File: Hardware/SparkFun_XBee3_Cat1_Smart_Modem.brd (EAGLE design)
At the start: 45.7 x 63.5 mm, 132 parts, among them J4 QWIIC_RIGHT_ANGLE, Q2 3.1A/30V/105mΩ, U1 FSUSB30MUX_MSOP10, U2 AP63203, U3 ESD Diode, U5 ESD Diode, U6 CP210X

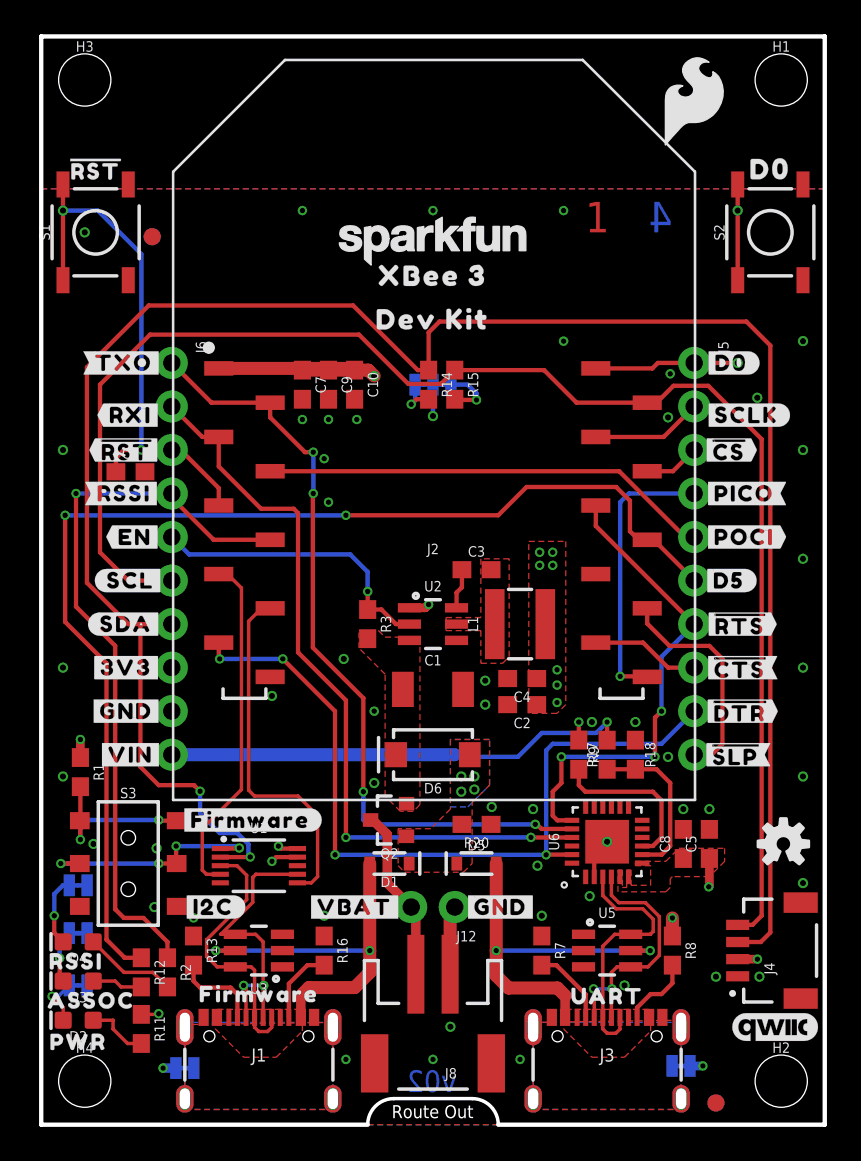
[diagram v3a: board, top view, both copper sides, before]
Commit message: NEW PINOUT - rearranges pinout to match module pinout directly
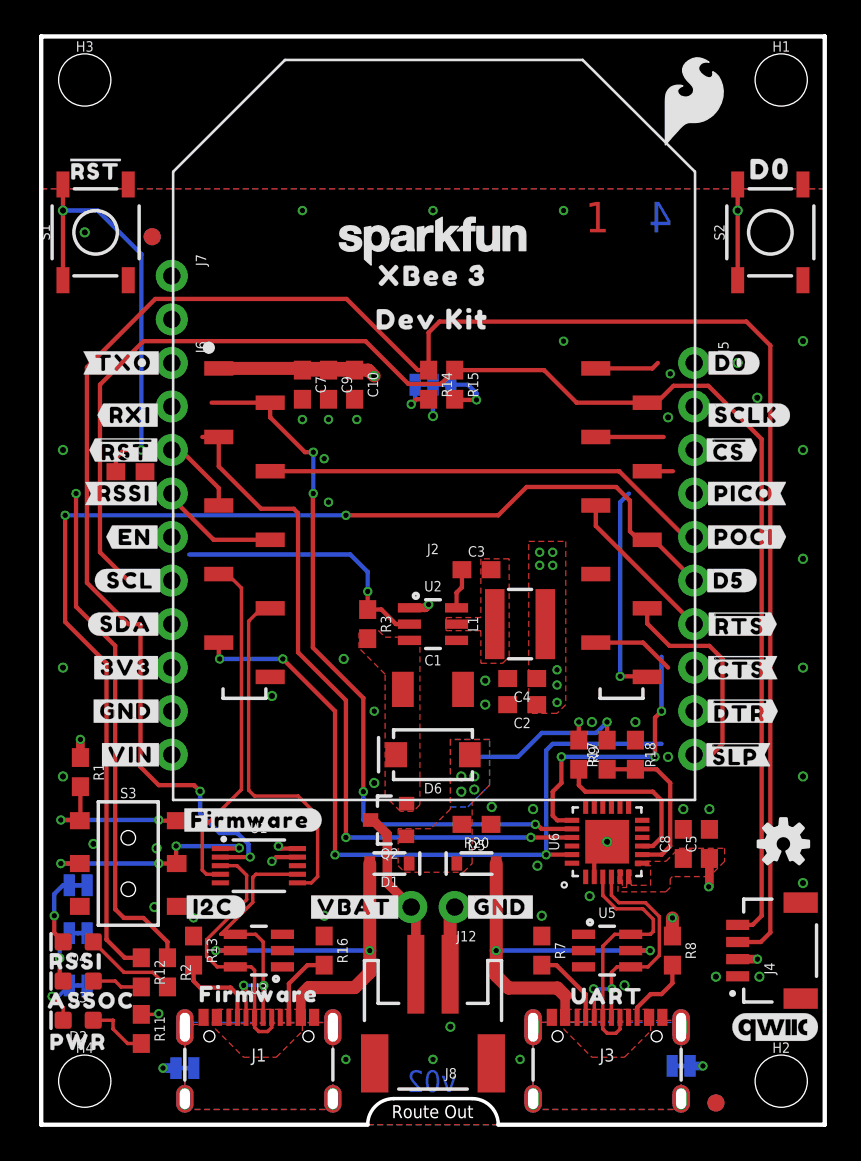
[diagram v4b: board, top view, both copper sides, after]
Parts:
- added J7: (no value), SparkFun-Connectors:1X02_NO_SILK
- moved U$64 4.76 mm to (2.16, 17.3), turned to 270 degrees
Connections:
- net !RESET!: now also J6.5; no longer J6.3
- net 3.3V: now also J6.1; no longer J6.8
- net D1/SCL: now also J5.2; no longer J6.6
- net D10/RSSI_PWM: now also J6.6; no longer J6.4
- net D12/SPI_POCI: now also J6.4; no longer J5.5
- net D13/TXO: now also J6.2; no longer J6.1
- net D14/RXI: now also J6.3; no longer J6.2
- net D2/SPI_CLK: now also J5.3; no longer J5.2
- net D3/SPI_!CS!: now also J5.4; no longer J5.3
- net D4/SPI_PICO: now also J5.10; no longer J5.4
- net D6/!RTS!: now also J5.5; no longer J5.7
- net D7/!CTS!: now also J5.9; no longer J5.8
- net D8/!DTR!: now also J6.9; no longer J5.9
- net D9/!SLEEP!: now also J5.8; no longer J5.10
- net EN: now also J7.1; no longer J6.5
- net GND: now also J6.10; no longer J6.9
- net VIN: now also J7.2; no longer J6.10
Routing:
- net VIN: track 25.8 -> 9.26 mm
- net D10/RSSI_PWM: track 42.6 -> 36.7 mm
- net D0: track 22.9 -> 18.2 mm
- net D4/SPI_PICO: track 16.3 -> 12.5 mm
- net D13/TXO: track 46.0 -> 42.7 mm
- net D1/SCL: track 87.9 -> 85.1 mm
- net D6/!RTS!: track 28.3 -> 25.6 mm
- net D8/!DTR!: track 46.9 -> 44.2 mm
- net D14/RXI: track 44.2 -> 41.7 mm
- net D2/SPI_CLK: track 6.48 -> 3.96 mm
- net !RESET!: track 31.6 -> 29.3 mm
- net D3/SPI_!CS!: track 3.25 -> 1.50 mm
- net D11/SDA: track 120.7 -> 119.1 mm
- net D7/!CTS!: track 6.34 -> 4.82 mm
- net EN: track 17.3 -> 15.8 mm
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
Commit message: Updates silk
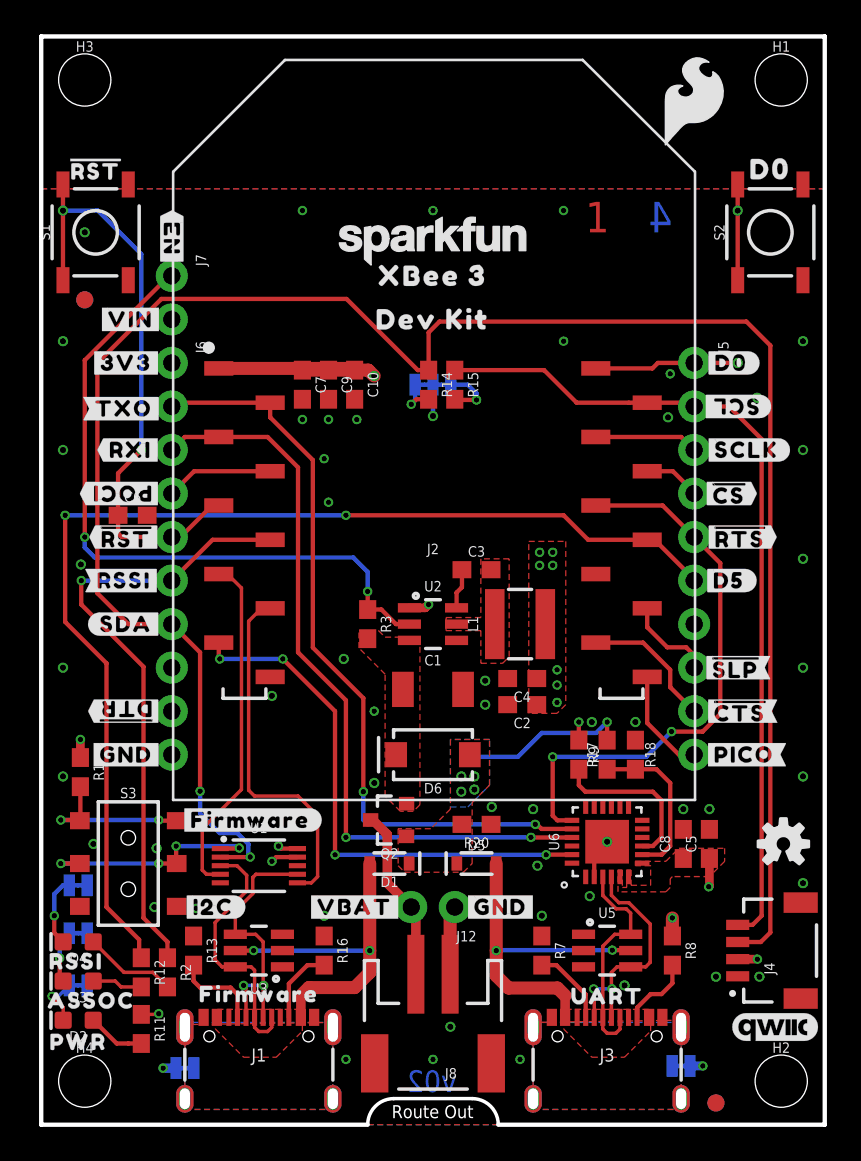
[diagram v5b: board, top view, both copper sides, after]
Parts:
- U$14: device top:#D12#POCI#23 -> top:#POCI#D12#24
- U$19: device top:#AD1#D1#7 -> top:#D1#AD1#8
- moved U$32 36.7 mm to (40.5, 41.9), turned to 180 degrees
- moved U$29 36.4 mm to (4.70, 36.8), turned to 180 degrees
- moved U$5 35.8 mm to (4.95, 24.1), turned to 180 degrees
- moved U$41 25.4 mm to (5.21, 47.0)
- moved U$46 25.4 mm to (10.0, 47.0)
- moved U$19 25.0 mm to (34.3, 41.9)
- moved U$59 22.4 mm to (11.6, 24.1)
- moved U$14 21.2 mm to (12.3, 36.8)
- moved U$44 17.8 mm to (10.3, 44.5)
- moved U$9 17.8 mm to (4.95, 44.5)
- moved U$24 17.5 mm to (7.62, 51.7), turned to 270 degrees
- moved U$21 15.2 mm to (9.78, 49.5)
- moved U$13 15.2 mm to (33.8, 21.6)
- moved U$28 15.2 mm to (41.0, 21.6)
- moved FD1 5.39 mm to (2.54, 48.1)
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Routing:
- net VIN: track 9.26 -> 52.2 mm
- net D1/SCL: track 85.1 -> 49.0 mm
- net EN: track 15.8 -> 40.1 mm, vias 1 -> 2
- net D12/SPI_POCI: track 25.8 -> 6.28 mm
- net D8/!DTR!: track 44.2 -> 36.4 mm
- net D6/!RTS!: track 25.6 -> 32.9 mm, vias 3 -> 2
- net D9/!SLEEP!: track 12.0 -> 5.24 mm
- net D4/SPI_PICO: track 12.5 -> 6.20 mm, vias 1 -> 0
- net !RESET!: track 29.3 -> 34.8 mm
- net D0: track 18.2 -> 22.9 mm
- net D7/!CTS!: track 4.82 -> 7.99 mm
- net D14/RXI: track 41.7 -> 44.4 mm
- net D+: track 15.3 -> 13.0 mm
- net V_USB_2: track 22.3 -> 20.0 mm
- net V_USB: track 22.4 -> 20.2 mm
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
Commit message: Updates a few labels
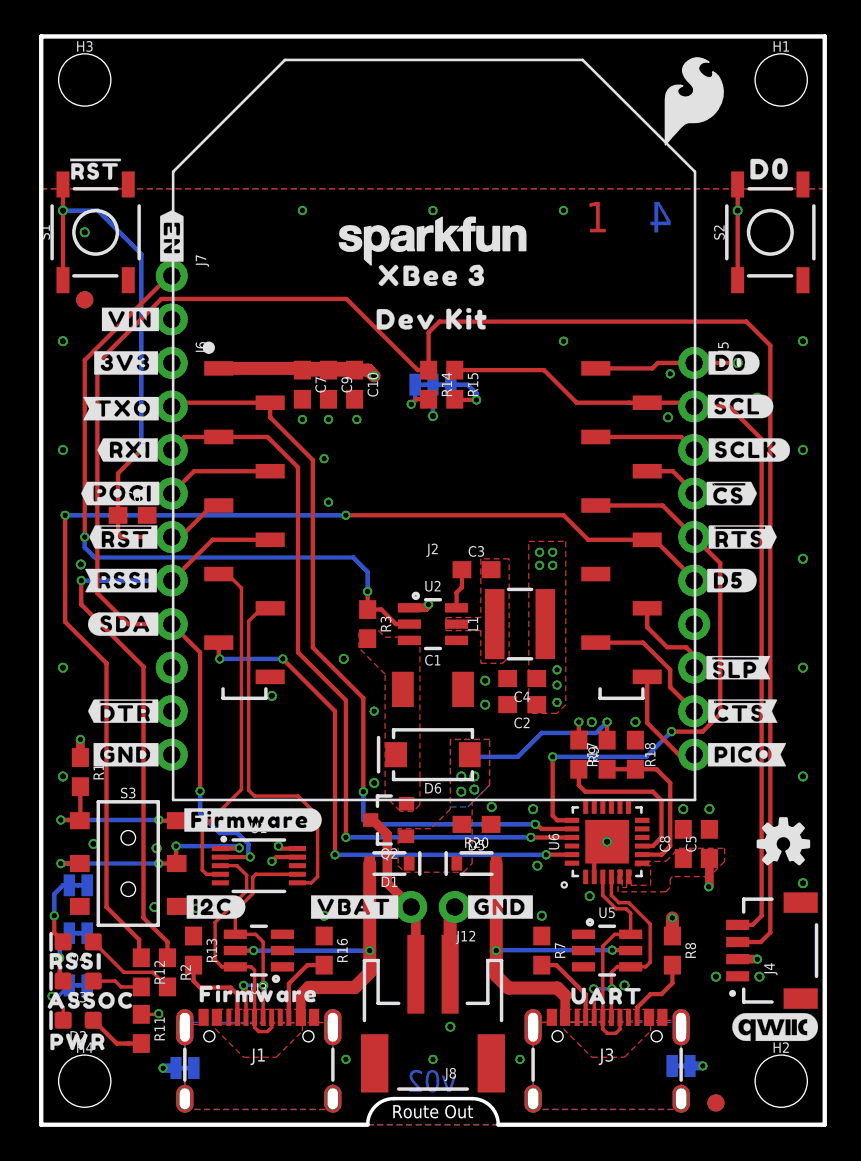
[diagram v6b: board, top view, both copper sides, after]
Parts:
- U$29: device top:#POCI#22 -> top:#POCI#23
- U$32: device top:#SCL#6 -> top:#SCL#7
- U$5: device top:##DTR##26 -> top:##DTR##27
- moved U$32 0.13 mm to (40.6, 41.9), turned to 0 degrees
- moved U$29 0.08 mm to (4.78, 36.8), turned to 0 degrees
- turned U$5 to 0 degrees
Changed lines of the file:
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@@
 <element name="U$3" library="top" package="##CS##19" value="" x="40.132" y="36.83" smashed="yes"/>
 <element name="U$4" library="top" package="##CTS##25" value="" x="40.767" y="24.13" smashed="yes"/>
-<element name="U$5" library="top" package="##DTR##26" value="" x="4.953" y="24.13" smashed="yes" rot="R180"/>
 <element name="U$7" library="top" package="##RTS##24" value="" x="40.767" y="34.29" smashed="yes"/>
 <element name="U$9" library="top" package="#3V3#1" value="" x="4.953" y="44.45" smashed="yes"/>
@@
 <element name="U$26" library="top" package="#I2C#33" value="" x="22.86" y="44.831" smashed="yes" rot="MR0"/>
 <element name="U$28" library="top" package="#PICO#23" value="" x="41.021" y="21.59" smashed="yes"/>
-<element name="U$29" library="top" package="#POCI#22" value="" x="4.699" y="36.83" smashed="yes" rot="R180"/>
 <element name="U$31" library="top" package="#RSSI#16" value="" x="4.826" y="31.75" smashed="yes"/>
-<element name="U$32" library="top" package="#SCL#6" value="" x="40.513" y="41.91" smashed="yes" rot="R180"/>
 <element name="U$33" library="top" package="#SCLK#18" value="" x="41.148" y="39.37" smashed="yes"/>
 <element name="U$34" library="top" package="#SDA#7" value="" x="4.953" y="29.21" smashed="yes"/>
@@
 <element name="U$19" library="top" package="#D1#AD1#8" value="" x="34.29" y="41.91" smashed="yes" rot="MR0"/>
 <element name="U$14" library="top" package="#POCI#D12#24" value="" x="12.319" y="36.83" smashed="yes" rot="MR0"/>
+<element name="U$29" library="top" package="#POCI#23" value="" x="4.7752" y="36.83" smashed="yes"/>
+<element name="U$32" library="top" package="#SCL#7" value="" x="40.64" y="41.91" smashed="yes"/>
+<element name="U$5" library="top" package="##DTR##27" value="" x="4.953" y="24.13" smashed="yes"/>
 </elements>
 <signals>

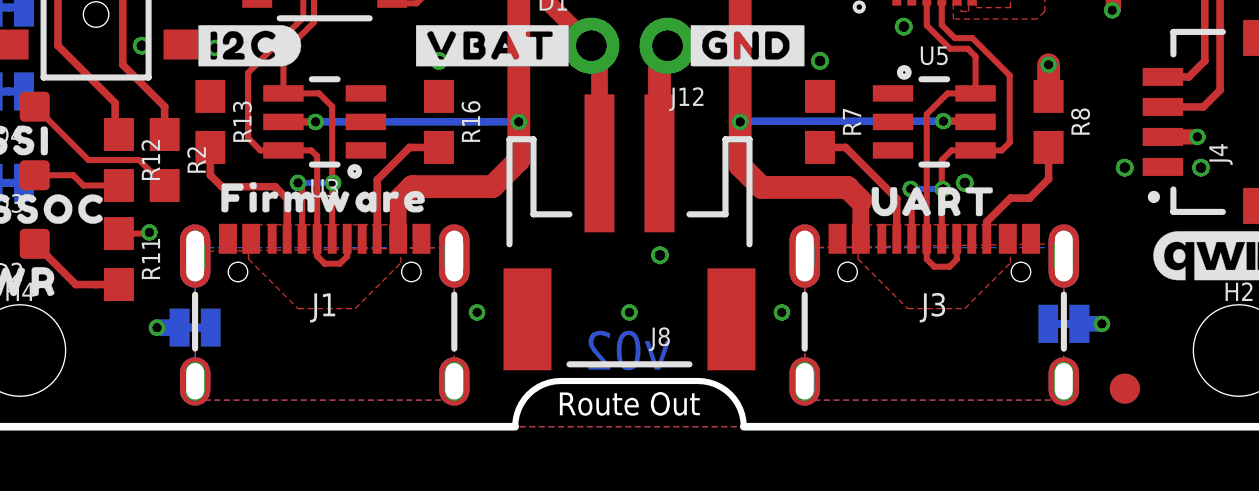
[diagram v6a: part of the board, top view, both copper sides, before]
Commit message: Replaces USB-C connector with four layer footprint
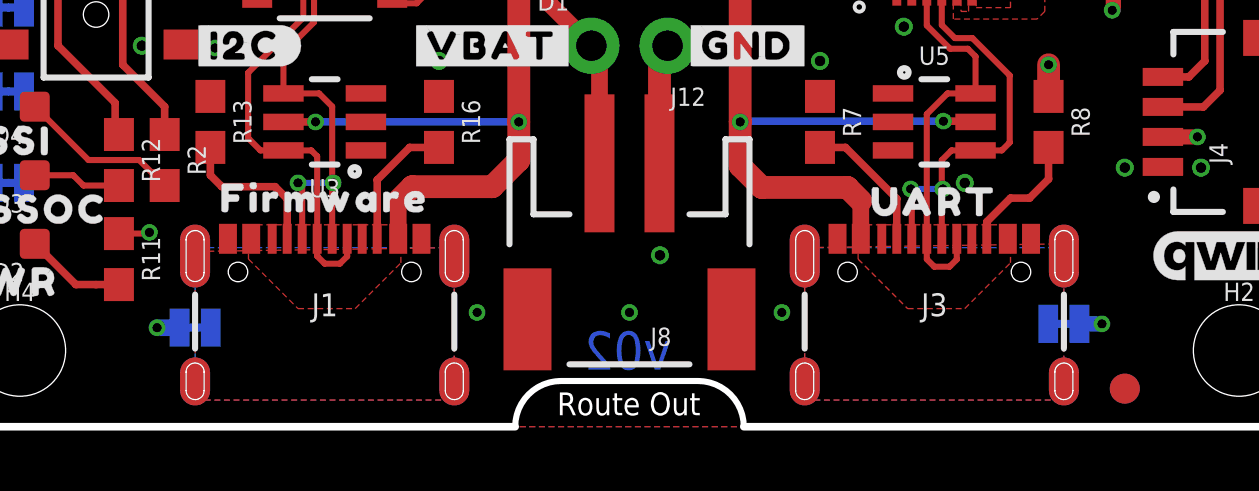
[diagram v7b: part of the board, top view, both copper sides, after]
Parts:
- J1, J3: value (none) -> USB Female Type C Connector; device SparkFun-Connectors:USB-C-16P-2LAYER-PADS -> SparkFun-Connectors:USB-C-16P-4LAYER-ISOLATED
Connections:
- net SHLD: now also J3.SHLD5, J3.SHLD6, J3.SHLD7, J3.SHLD8
- net SHLD1: now also J1.SHLD5, J1.SHLD6, J1.SHLD7, J1.SHLD8
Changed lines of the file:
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@@
 <setting verticaltext="up"/>
 </settings>
-<grid distance="0.05" unitdist="inch" unit="inch" style="dots" multiple="1" display="yes" altdistance="0.001" altunitdist="inch" altunit="inch"/>
+<grid distance="0.05" unitdist="inch" unit="inch" style="dots" multiple="1" display="yes" altdistance="0.005" altunitdist="inch" altunit="inch"/>
 <layers>
 <layer number="1" name="Top" color="4" fill="1" visible="yes" active="yes"/>
@@
 <layer number="115" name="ReferenceISLANDS" color="7" fill="1" visible="no" active="yes"/>
 <layer number="116" name="Patch_BOT" color="9" fill="4" visible="no" active="yes"/>
-<layer number="117" name="PM_Ref" color="26" fill="1" visible="no" active="yes"/>
+<layer number="117" name="PM_Ref" color="26" fill="1" visible="yes" active="yes"/>
 <layer number="118" name="Rect_Pads" color="7" fill="1" visible="no" active="yes"/>
-<layer number="119" name="PF_Ref" color="31" fill="1" visible="no" active="yes"/>
-<layer number="120" name="WFL_Ref" color="25" fill="1" visible="no" active="yes"/>
+<layer number="119" name="PF_Ref" color="31" fill="1" visible="yes" active="yes"/>
+<layer number="120" name="WFL_Ref" color="25" fill="1" visible="yes" active="yes"/>
 <layer number="121" name="_tsilk" color="7" fill="1" visible="no" active="yes"/>
 <layer number="122" name="_bsilk" color="7" fill="1" visible="no" active="yes"/>
@@
 <attribute name="VALUE" x="23.368" y="43.18" size="0.6096" layer="27" font="vector" ratio="20" rot="R270" align="top-center"/>
 </element>
-<element name="J3" library="SparkFun-Connectors" package="USB-C-16P-2LAYER-PADS" value="" x="33.02" y="6.604" smashed="yes">
+<element name="J3" library="SparkFun-Connectors" package="USB-C-16P-4LAYER-ISOLATED" value="USB Female Type C Connector" x="33.02" y="6.604" smashed="yes">
 <attribute name="NAME" x="33.02" y="4.064" size="0.762" layer="25" align="center"/>
 <attribute name="PROD_ID" value="CONN-14122" x="33.02" y="7.874" size="1.778" layer="27" font="vector" ratio="15" display="off"/>
-<attribute name="VALUE" x="33.02" y="2.794" size="0.762" layer="27" align="center"/>
+<attribute name="VALUE" value="USB Female Type C Connector" x="33.02" y="2.794" size="0.762" layer="27" align="center"/>
 </element>
 <element name="R7" library="SparkFun-Resistors" package="0603" value="5.1k" x="29.21" y="10.16" smashed="yes" rot="R270">
@@
 <attribute name="VALUE" x="12.7" y="12.573" size="0.6096" layer="27" font="vector" ratio="20" align="bottom-center"/>
 </element>
-<element name="J1" library="SparkFun-Connectors" package="USB-C-16P-2LAYER-PADS" value="" x="12.7" y="6.604" smashed="yes">
+<element name="J1" library="SparkFun-Connectors" package="USB-C-16P-4LAYER-ISOLATED" value="USB Female Type C Connector" x="12.7" y="6.604" smashed="yes">
 <attribute name="NAME" x="12.7" y="4.064" size="0.762" layer="25" align="center"/>
 <attribute name="PROD_ID" value="CONN-14122" x="12.7" y="9.144" size="1.778" layer="27" display="off"/>
-<attribute name="VALUE" x="12.7" y="2.794" size="0.762" layer="27" align="center"/>
+<attribute name="VALUE" value="USB Female Type C Connector" x="12.7" y="2.794" size="0.762" layer="27" align="center"/>
 </element>
 <element name="R13" library="SparkFun-Resistors" package="0603" value="5.1k" x="8.89" y="10.16" smashed="yes" rot="R270">
@@
 <vertex x="37.338" y="5.969"/>
 </polygon>
+<contactref element="J3" pad="SHLD5"/>
+<contactref element="J3" pad="SHLD6"/>
+<contactref element="J3" pad="SHLD7"/>
+<contactref element="J3" pad="SHLD8"/>
+<wire x1="37.34" y1="5.689" x2="37.34" y2="5.689" width="0" layer="19" extent="1-16"/>
+<wire x1="28.7" y1="5.689" x2="28.7" y2="5.689" width="0" layer="19" extent="1-16"/>
+<wire x1="28.7" y1="1.509" x2="28.7" y2="1.509" width="0" layer="19" extent="1-16"/>
 </signal>
 <signal name="D+" class="2">
@@
 <vertex x="17.018" y="5.969"/>
 </polygon>
+<contactref element="J1" pad="SHLD5"/>
+<contactref element="J1" pad="SHLD6"/>
+<contactref element="J1" pad="SHLD7"/>
+<contactref element="J1" pad="SHLD8"/>
+<wire x1="17.02" y1="5.689" x2="17.02" y2="5.689" width="0" layer="19" extent="1-16"/>
+<wire x1="8.38" y1="5.689" x2="8.38" y2="5.689" width="0" layer="19" extent="1-16"/>
+<wire x1="8.38" y1="1.509" x2="8.38" y2="1.509" width="0" layer="19" extent="1-16"/>
 </signal>
 <signal name="DIRECT_SELECT">
